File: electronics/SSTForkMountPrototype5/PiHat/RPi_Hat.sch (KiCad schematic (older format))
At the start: 32 parts, among them CON1 BARREL_JACK, J1 RJ12, J4 Screw_Terminal_01x08, J5 Screw_Terminal_01x03, Q1 Q_NPN_BEC, Q2 Q_NPN_BEC, Q3 Q_NPN_BEC, SW1 SW_SPST, U1 MCQ9435, U2 pololu_D24V22F5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

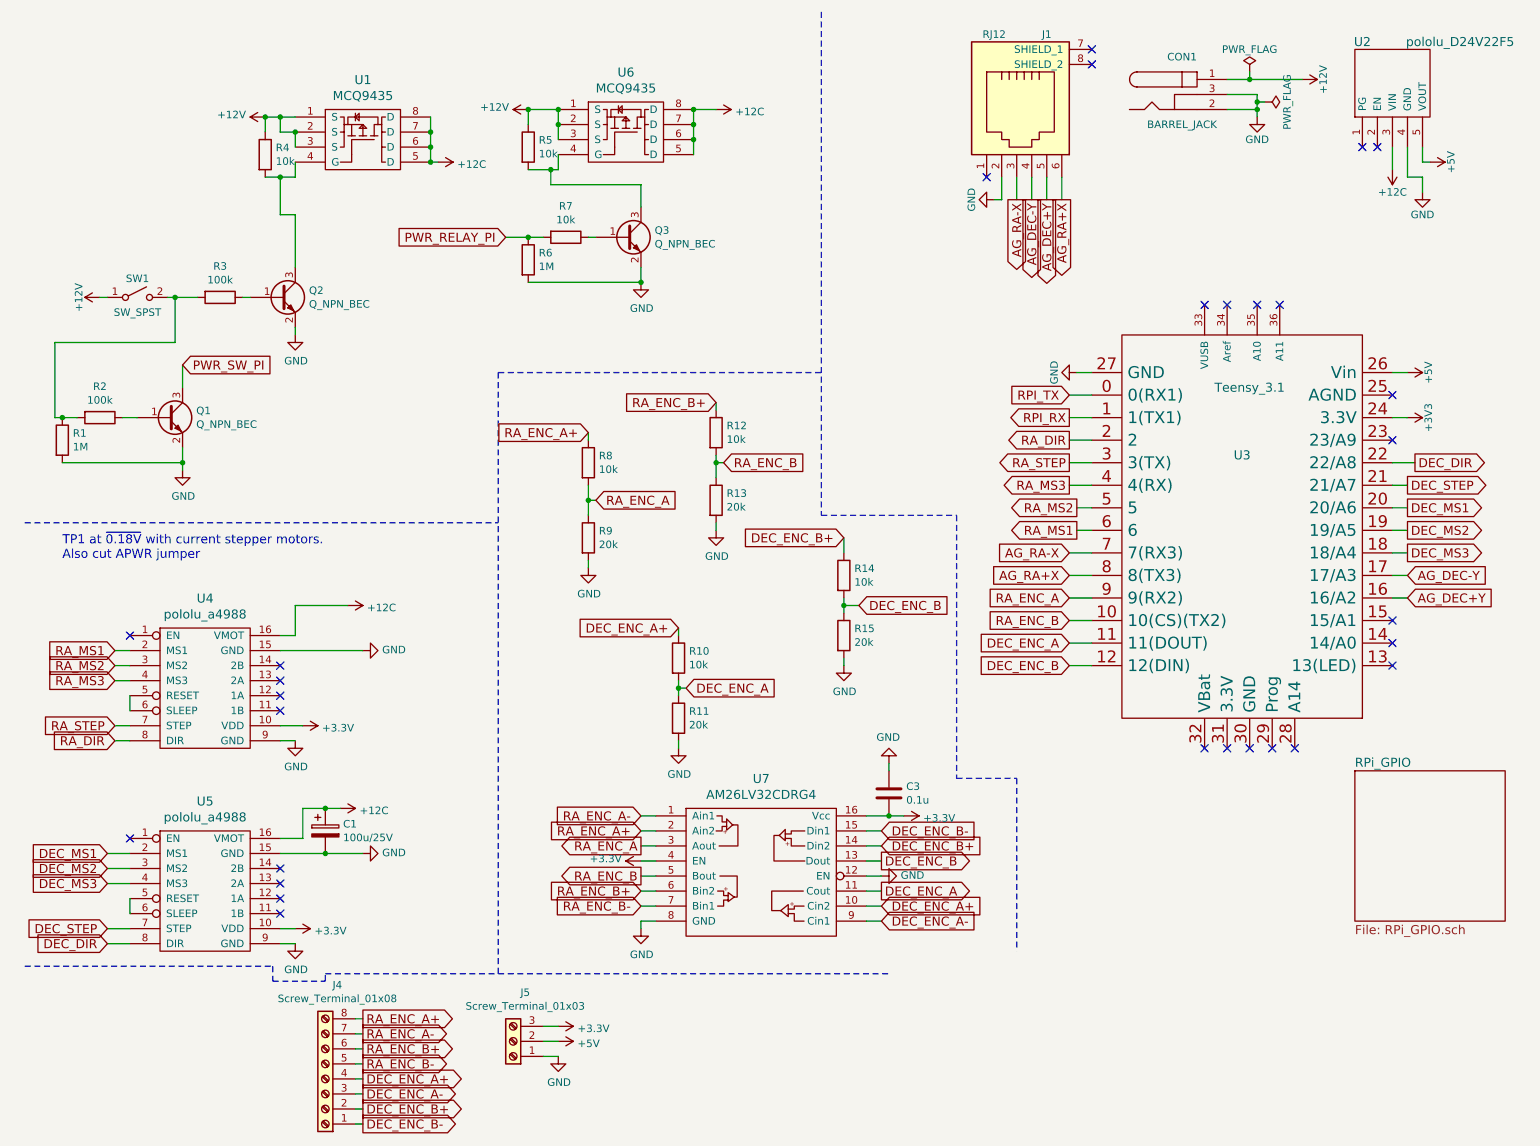
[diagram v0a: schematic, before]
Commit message: Removed mosfet switching. Seperate DEC/RA encoder headers.
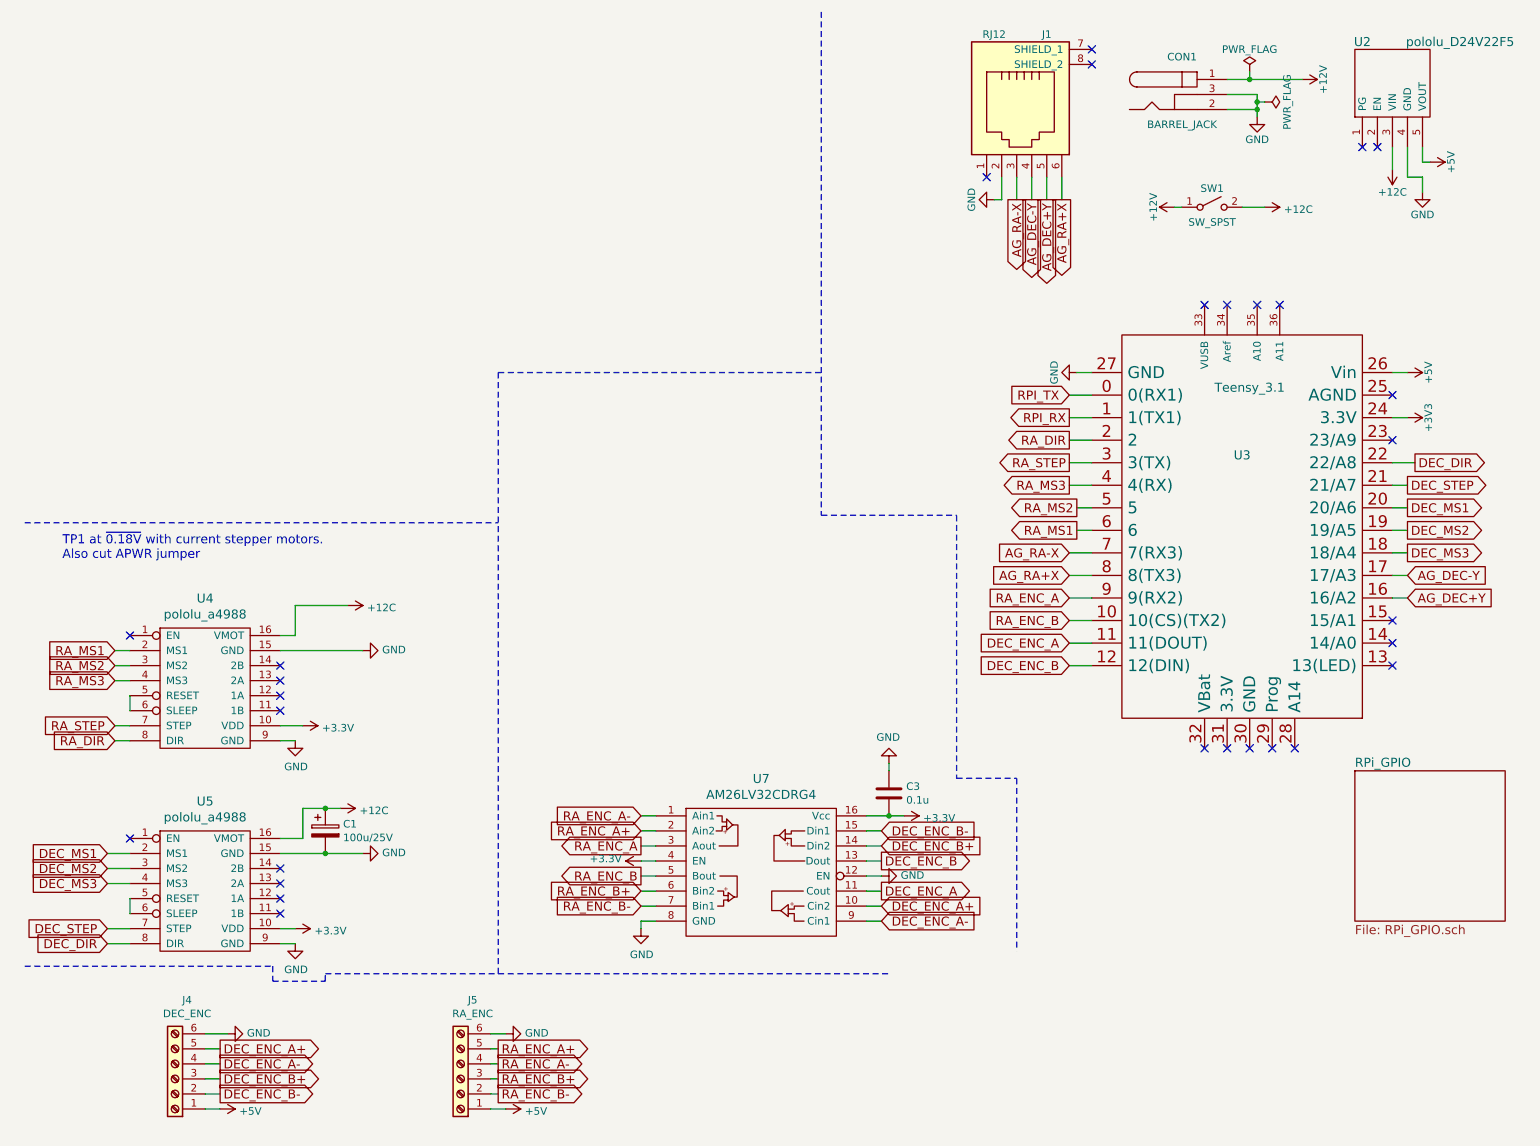
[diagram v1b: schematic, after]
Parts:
- removed J4: Screw_Terminal_01x08, Connectors:1X08_LOCK_LONGPADS, symbol Connector:Screw_Terminal_01x08
- removed J5: Screw_Terminal_01x03, Connectors:1X03_LOCK_LONGPADS, symbol Connector:Screw_Terminal_01x03
- removed Q1, Q2, Q3: Q_NPN_BEC, TO_SOT_Packages_SMD:SOT-23, symbol Device:Q_NPN_BEC
- removed R1, R6: 1M, Resistors_SMD:R_0603, symbol Device:R
- removed R10, R12, R14, R4, R5, R7, R8: 10k, Resistors_SMD:R_0603, symbol Device:R
- removed R11, R13, R15, R9: 20k, Resistors_SMD:R_0603, symbol Device:R
- removed R2, R3: 100k, Resistors_SMD:R_0603, symbol Device:R
- removed U1, U6: MCQ9435, Housings_SOIC:SOIC-8_3.9x4.9mm_Pitch1.27mm, symbol SST_kicad_sym:MCQ9435
- added J4: DEC_ENC, Connectors:1X06_LOCK_LONGPADS, symbol Connector:Screw_Terminal_01x06
- added J5: RA_ENC, Connectors:1X06_LOCK_LONGPADS, symbol Connector:Screw_Terminal_01x06
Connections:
- net +12C: now also SW1.2 (B)
- net +5V: now also J4.1 (Pin_1), J5.1 (Pin_1)
- net DEC_ENC_A+: now also J4.5 (Pin_5)
- net DEC_ENC_A-: now also J4.4 (Pin_4)
- net DEC_ENC_B+: now also J4.3 (Pin_3)
- net DEC_ENC_B-: now also J4.2 (Pin_2)
- net GND: now also J4.6 (Pin_6), J5.6 (Pin_6)
- net RA_ENC_A+: now also J5.5 (Pin_5)
- net RA_ENC_A-: now also J5.4 (Pin_4)
- net RA_ENC_B+: now also J5.3 (Pin_3)
- net RA_ENC_B-: now also J5.2 (Pin_2)
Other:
- moved on the sheet: SW1

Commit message: Fixed negative inputs. Fixed HADec no tracking status. Fixed infinite slew. Added reverse voltage mosfet.
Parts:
- added Q1: Si2369DS, Package_TO_SOT_SMD:SOT-23, symbol Device:Q_PMOS_GSD
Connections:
- net +12C: now also Q1.2 (S); no longer SW1.2 (B)
- net GND: now also Q1.1 (G)
- new net: Q1.3 (D), SW1.2 (B)
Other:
- moved on the sheet: SW1
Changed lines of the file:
@@
 EESchema Schematic File Version 4
-LIBS:RPi_Hat-cache
-EELAYER 26 0
+EELAYER 30 0
 EELAYER END
 $Descr USLetter 11000 8500
@@
 Sheet 1 2
 Title "SSTEQ25"
-Date "2020-06-06"
-Rev "0.1.0"
+Date "2020-12-18"
+Rev "0.1.1"
 Comp "StarSync Trackers"
 Comment1 ""
@@
 L RPi_Hat-rescue:SW_SPST SW1
 U 1 1 5B6F8977
-P 8400 1800
-F 0 "SW1" H 8400 1925 50  0000 C CNN
-F 1 "SW_SPST" H 8400 1700 50  0000 C CNN
-F 2 "custom_footprints:PWR_SWITCH_RA1H1C112R" H 8400 1800 50  0001 C CNN
-F 3 "" H 8400 1800 50  0001 C CNN
-	1    8400 1800
+P 8050 1700
+F 0 "SW1" H 8050 1825 50  0000 C CNN
+F 1 "SW_SPST" H 8050 1600 50  0000 C CNN
+F 2 "custom_footprints:PWR_SWITCH_RA1H1C112R" H 8050 1700 50  0001 C CNN
+F 3 "" H 8050 1700 50  0001 C CNN
+	1    8050 1700
 	1    0    0    -1
 $EndComp
@@
 L RPi_Hat-rescue:+12V #PWR019
 U 1 1 5B6F90E6
-P 8150 1800
-F 0 "#PWR019" H 8150 1650 50  0001 C CNN
-F 1 "+12V" H 8150 1940 50  0000 C CNN
-F 2 "" H 8150 1800 50  0001 C CNN
-F 3 "" H 8150 1800 50  0001 C CNN
-	1    8150 1800
+P 7800 1700
+F 0 "#PWR019" H 7800 1550 50  0001 C CNN
+F 1 "+12V" H 7800 1840 50  0000 C CNN
+F 2 "" H 7800 1700 50  0001 C CNN
+F 3 "" H 7800 1700 50  0001 C CNN
+	1    7800 1700
 	0    -1   -1   0
 $EndComp
 Wire Wire Line
-	8150 1800 8200 1800
+	7800 1700 7850 1700
 $Comp
 L RPi_Hat-rescue:+12C #PWR031
@@
 L power:+12C #PWR0112
 U 1 1 5C8E340B
-P 8750 1800
-F 0 "#PWR0112" H 8750 1650 50  0001 C CNN
-F 1 "+12C" V 8765 1928 50  0000 L CNN
-F 2 "" H 8750 1800 50  0001 C CNN
-F 3 "" H 8750 1800 50  0001 C CNN
-	1    8750 1800
+P 8950 1700
+F 0 "#PWR0112" H 8950 1550 50  0001 C CNN
+F 1 "+12C" V 8965 1828 50  0000 L CNN
+F 2 "" H 8950 1700 50  0001 C CNN
+F 3 "" H 8950 1700 50  0001 C CNN
+	1    8950 1700
 	0    1    1    0
 $EndComp
@@
 $EndComp
 Wire Wire Line
-	8600 1800 8750 1800
+	8250 1700 8400 1700
 $Comp
 L Connector:Screw_Terminal_01x06 J4
@@
 Wire Wire Line
 	1700 7700 1800 7700
+$Comp
+L Device:Q_PMOS_GSD Q1
+U 1 1 5FDD871D
+P 8600 1800
+F 0 "Q1" V 8942 1800 50  0000 C CNN
+F 1 "Si2369DS" V 8851 1800 50  0000 C CNN
+F 2 "Package_TO_SOT_SMD:SOT-23" H 8800 1900 50  0001 C CNN
+F 3 "~" H 8600 1800 50  0001 C CNN
+	1    8600 1800
+	0    -1   -1   0
+$EndComp
+Wire Wire Line
+	8800 1700 8950 1700
+$Comp
+L power:GND #PWR0114
+U 1 1 5FE0AAA1
+P 8600 2050
+F 0 "#PWR0114" H 8600 1800 50  0001 C CNN
+F 1 "GND" H 8605 1877 50  0000 C CNN
+F 2 "" H 8600 2050 50  0001 C CNN
+F 3 "" H 8600 2050 50  0001 C CNN
+	1    8600 2050
+	1    0    0    -1
+$EndComp
+Wire Wire Line
+	8600 2000 8600 2050
 $EndSCHEMATC

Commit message: Removed note about jummper cut, was for older drivers.
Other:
- note added: "Add 100uF/25V through hole on \nVMOT and GND on each driver."
- note added: "TP1 at ~0.18V with current stepper motors."
- note removed: "TP1 at ~0.18V with current stepper motors.\nAlso cut APWR jumper"
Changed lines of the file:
@@
 Sheet 1 2
 Title "SSTEQ25"
-Date "2020-12-18"
-Rev "0.1.1"
+Date "2021-01-04"
+Rev "0.1.2"
 Comp "StarSync Trackers"
 Comment1 ""
@@
 $EndComp
 Text Notes 750  4150 0    60   ~ 0
-TP1 at ~0.18V with current stepper motors.\nAlso cut APWR jumper
+TP1 at ~0.18V with current stepper motors.
 Wire Wire Line
 	8700 1150 8700 1200
@@
 Wire Notes Line
 	5800 500  5800 3850
-Wire Wire Line
-	2300 4450 2650 4450
-Wire Wire Line
-	2200 4750 2750 4750
 NoConn ~ 2200 6200
 NoConn ~ 2200 6300
@@
 Wire Wire Line
 	8600 2000 8600 2050
+Wire Wire Line
+	2300 4450 2650 4450
+Wire Wire Line
+	2200 4750 2750 4750
+Text Notes 2450 5600 0    60   ~ 0
+Add 100uF/25V through hole on \nVMOT and GND on each driver.
 $EndSCHEMATC
